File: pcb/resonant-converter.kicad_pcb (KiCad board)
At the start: 2 copper layers, 0 parts

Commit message: PCB: Setup PCB stackup, DRC and pre-defined sizes
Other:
- board outline added: 100 x 100 mm
- copper layers 2 -> 4
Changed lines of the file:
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@@
 	(generator_version "9.0")
 	(general
-		(thickness 1.6)
+		(thickness 1.6062)
 		(legacy_teardrops no)
 	)
@@
 	(layers
 		(0 "F.Cu" signal)
+		(4 "In1.Cu" signal)
+		(6 "In2.Cu" signal)
 		(2 "B.Cu" signal)
 		(9 "F.Adhes" user "F.Adhesive")
@@
 		(43 "User.3" user)
 		(45 "User.4" user)
+		(47 "User.5" user)
+		(49 "User.6" user)
+		(51 "User.7" user)
+		(53 "User.8" user)
+		(55 "User.9" user)
 	)
 	(setup
+		(stackup
+			(layer "F.SilkS"
+				(type "Top Silk Screen")
+				(color "White")
+			)
+			(layer "F.Paste"
+				(type "Top Solder Paste")
+			)
+			(layer "F.Mask"
+				(type "Top Solder Mask")
+				(color "Black")
+				(thickness 0.01)
+			)
+			(layer "F.Cu"
+				(type "copper")
+				(thickness 0.035)
+			)
+			(layer "dielectric 1"
+				(type "prepreg")
+				(color "FR4 natural")
+				(thickness 0.2104)
+				(material "FR4")
+				(epsilon_r 4.4)
+				(loss_tangent 0.02)
+			)
+			(layer "In1.Cu"
+				(type "copper")
+				(thickness 0.0152)
+			)
+			(layer "dielectric 2"
+				(type "core")
+				(color "FR4 natural")
+				(thickness 1.065)
+				(material "FR4")
+				(epsilon_r 4.6)
+				(loss_tangent 0.02)
+			)
+			(layer "In2.Cu"
+				(type "copper")
+				(thickness 0.0152)
+			)
+			(layer "dielectric 3"
+				(type "prepreg")
+				(color "FR4 natural")
+				(thickness 0.2104)
+				(material "FR4")
+				(epsilon_r 4.4)
+				(loss_tangent 0.02)
+			)
+			(layer "B.Cu"
+				(type "copper")
+				(thickness 0.035)
+			)
+			(layer "B.Mask"
+				(type "Bottom Solder Mask")
+				(color "Black")
+				(thickness 0.01)
+			)
+			(layer "B.Paste"
+				(type "Bottom Solder Paste")
+			)
+			(layer "B.SilkS"
+				(type "Bottom Silk Screen")
+				(color "White")
+			)
+			(copper_finish "None")
+			(dielectric_constraints no)
+		)
 		(pad_to_mask_clearance 0)
 		(allow_soldermask_bridges_in_footprints no)
@@
 	)
 	(net 0 "")
+	(gr_rect
+		(start 100 50)
+		(end 200 150)
+		(stroke
+			(width 0.05)
+			(type solid)
+		)
+		(fill no)
+		(layer "Edge.Cuts")
+	)
 	(embedded_fonts no)
 )

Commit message: WIP: Create PCB mockup
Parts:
- added J1: Banana_Jack_Keystone_575-8, DW-footprints:Conn_Banana_Jack_Keystone_575-8, F.Cu at (106.0, 90.0)
- added J2: Banana_Jack_Keystone_575-8, DW-footprints:Conn_Banana_Jack_Keystone_575-8, F.Cu at (106.0, 110.0)
- added J3: Banana_Jack_Keystone_575-8, DW-footprints:Conn_Banana_Jack_Keystone_575-8, F.Cu at (195.0, 90.0)
- added J4: Banana_Jack_Keystone_575-8, DW-footprints:Conn_Banana_Jack_Keystone_575-8, F.Cu at (195.0, 110.0)
- added Q1: SIS472DN-T1-GE3, DW-footprints:PowerPAK-1212-8_Single, F.Cu at (134.4, 100.3)
- added Q2: SIS472DN-T1-GE3, DW-footprints:PowerPAK-1212-8_Single, F.Cu at (134.4, 105.0)
- added Q3: SIS472DN-T1-GE3, DW-footprints:PowerPAK-1212-8_Single, F.Cu at (169.4, 105.0)
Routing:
- added copper zone on In1.Cu, net GND
- added copper zone on In2.Cu, net GND

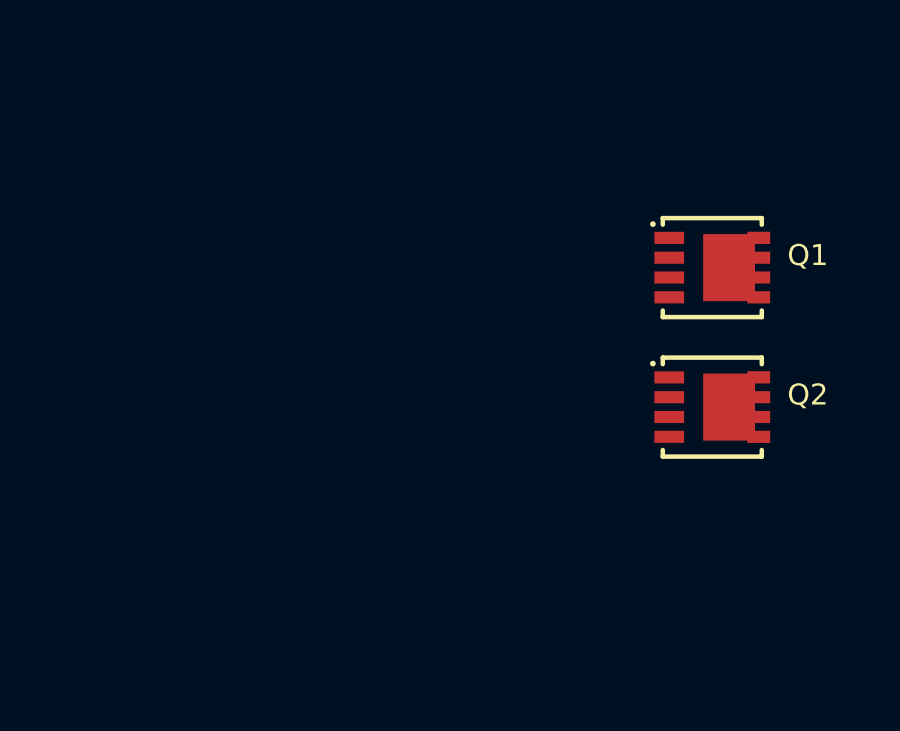
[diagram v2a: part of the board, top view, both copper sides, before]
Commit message: Add LLC controller IC
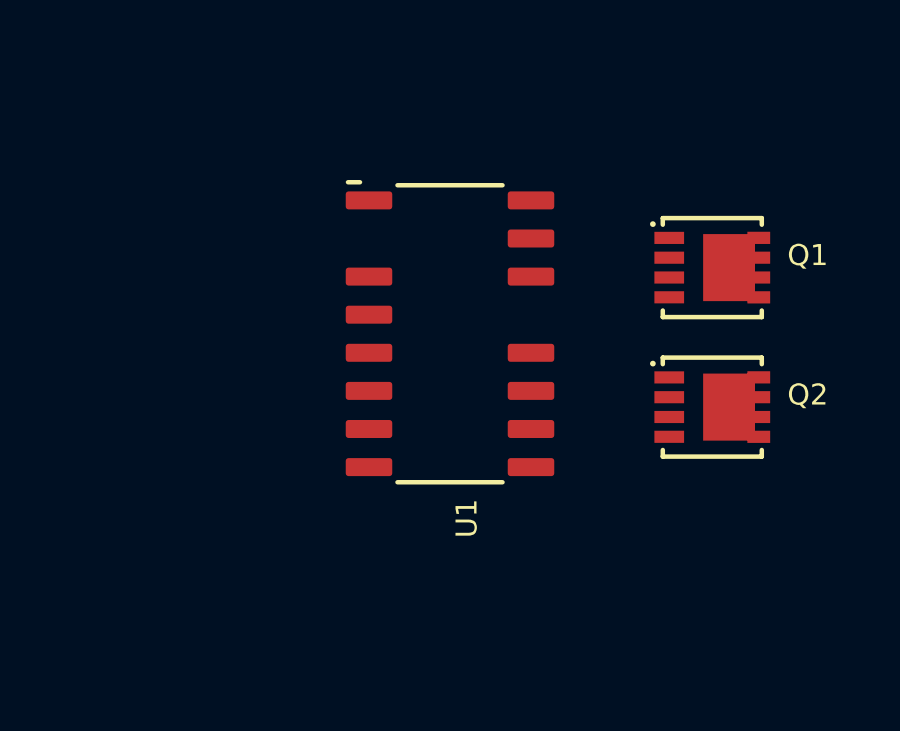
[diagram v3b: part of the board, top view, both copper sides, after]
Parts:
- added U1: UCC256610DDBR, DW-footprints:DDB0014A, F.Cu at (125.7, 102.6)

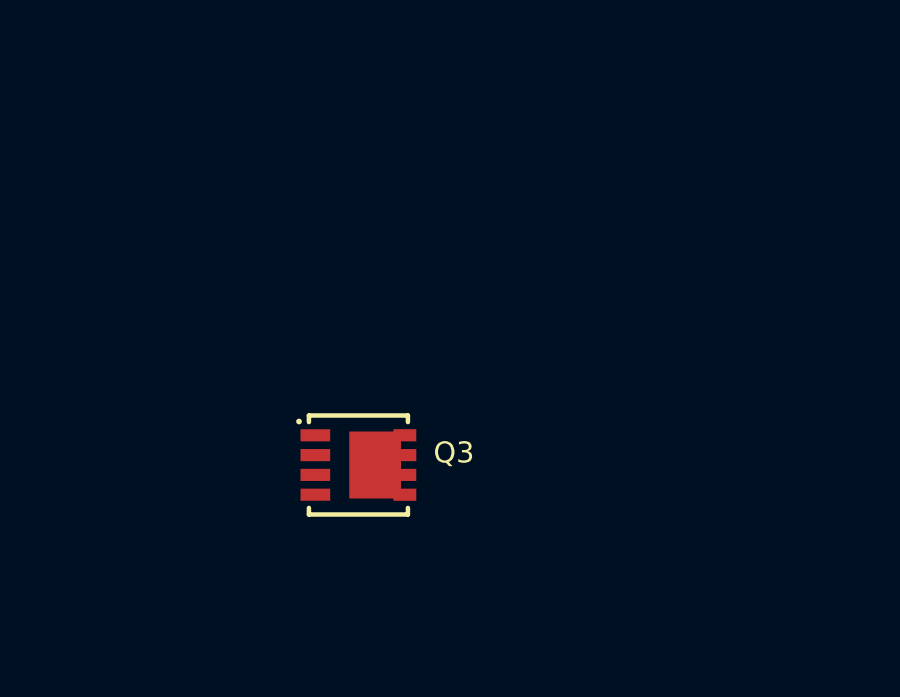
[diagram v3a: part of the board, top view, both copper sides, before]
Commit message: Add output rectifier schottky diodes
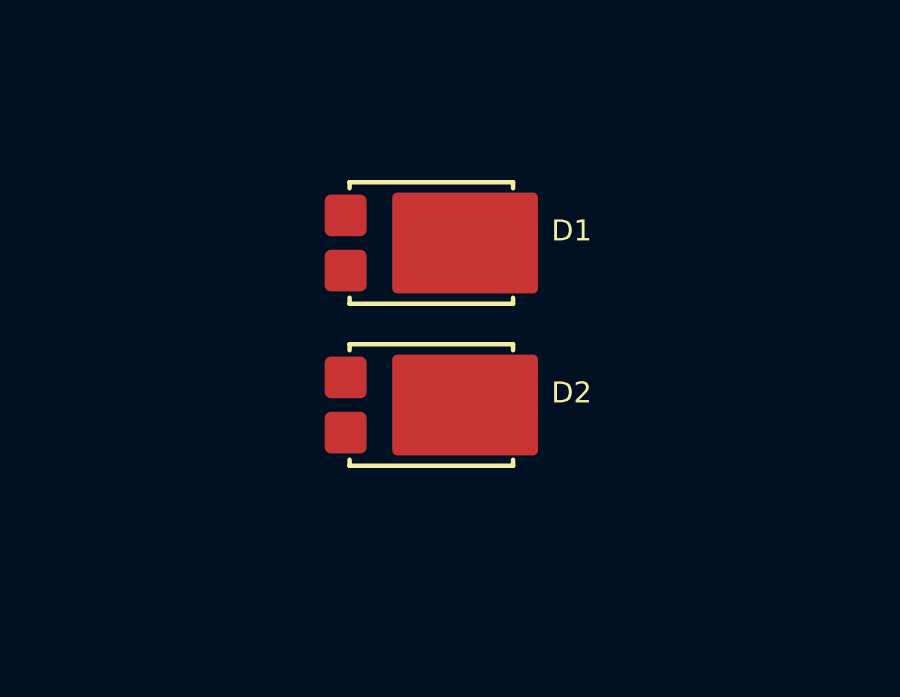
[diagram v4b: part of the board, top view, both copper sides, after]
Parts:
- removed Q3: SIS472DN-T1-GE3, DW-footprints:PowerPAK-1212-8_Single
- added D1: SBRT15U50SP5-13, DW-footprints:PowerDI-5, F.Cu at (171.9, 97.6)
- added D2: SBRT15U50SP5-13, DW-footprints:PowerDI-5, F.Cu at (171.9, 103.0)

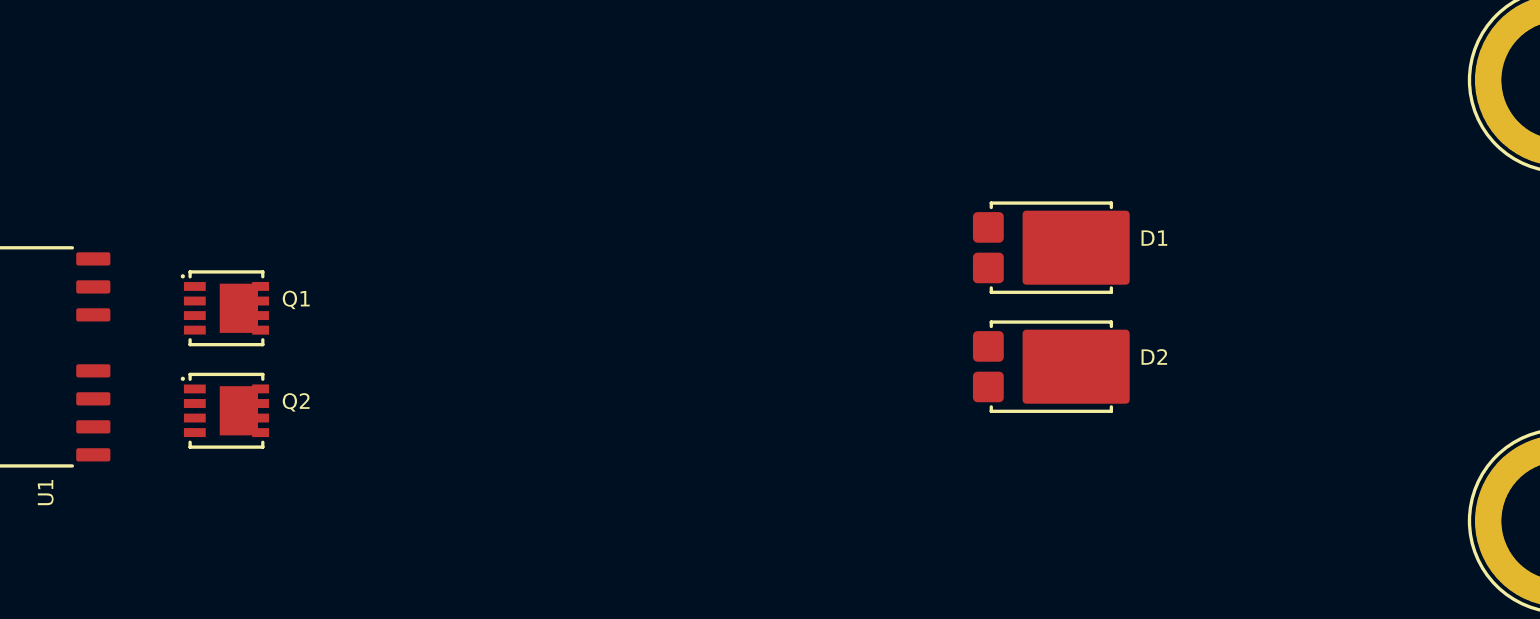
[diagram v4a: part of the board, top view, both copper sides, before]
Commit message: Add synchronous rectifier
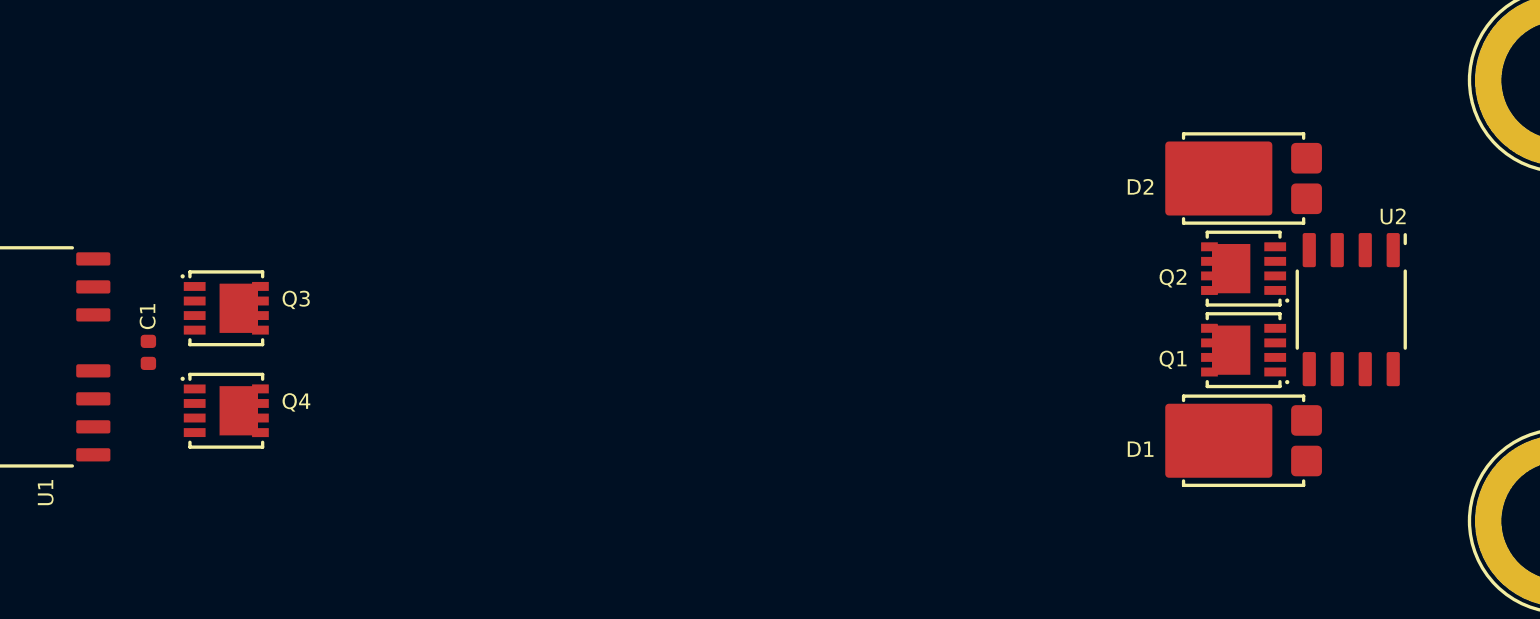
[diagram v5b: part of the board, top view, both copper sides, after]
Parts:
- added C1: C-1u-0402, DW-footprints:C_0402_1005Metric, F.Cu at (130.9, 102.3)
- added Q3: SIS472DN-T1-GE3, DW-footprints:PowerPAK-1212-8_Single, F.Cu at (134.4, 100.3)
- added Q4: SIS472DN-T1-GE3, DW-footprints:PowerPAK-1212-8_Single, F.Cu at (134.4, 105.0)
- added U2: TEA2096T/1J, DW-footprints:SOIC-8_3.9x4.9mm_P1.27mm, F.Cu at (185.5, 100.4)
- moved Q2 46.6 mm to (180.6, 98.5), turned to 180 degrees
- moved Q1 46.2 mm to (180.6, 102.2), turned to 180 degrees
- moved D1 12.4 mm to (180.6, 106.4), turned to 180 degrees
- moved D2 12.2 mm to (180.6, 94.5), turned to 180 degrees
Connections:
- D1 pad 1: unconnected-(D1-C-Pad1) -> Net-(D1-C)
- D1 pad 2: unconnected-(D1-A-Pad2) -> GND
- D2 pad 1: unconnected-(D2-C-Pad1) -> Net-(D2-C)
- D2 pad 2: unconnected-(D2-A-Pad2) -> GND
- J1 pad 1: unconnected-(J1-Pad1) -> VCC
- J2 pad 1: unconnected-(J2-Pad1) -> GNDPWR
- J3 pad 1: unconnected-(J3-Pad1) -> +12V
- Q1 pad 1: Net-(Q1-S-Pad1) -> GND
- Q1 pad 2: Net-(Q1-S-Pad1) -> GND
- Q1 pad 3: Net-(Q1-S-Pad1) -> GND
- Q1 pad 4: unconnected-(Q1-G-Pad4) -> Net-(Q1-G)
- Q1 pad 5: unconnected-(Q1-D-Pad5) -> Net-(D1-C)
- Q2 pad 1: Net-(Q2-S-Pad1) -> GND
- Q2 pad 2: Net-(Q2-S-Pad1) -> GND
- Q2 pad 3: Net-(Q2-S-Pad1) -> GND
- Q2 pad 4: unconnected-(Q2-G-Pad4) -> Net-(Q2-G)
- Q2 pad 5: unconnected-(Q2-D-Pad5) -> Net-(D2-C)
- U1 pad 10: unconnected-(U1-GNDP-Pad10) -> GNDPWR
- U1 pad 11: unconnected-(U1-LO-Pad11) -> Net-(Q4-G)
- U1 pad 14: unconnected-(U1-HB-Pad14) -> Net-(U1-HB)
- U1 pad 15: unconnected-(U1-HO-Pad15) -> Net-(Q3-G)
- U1 pad 16: unconnected-(U1-HS-Pad16) -> Net-(Q4-D)

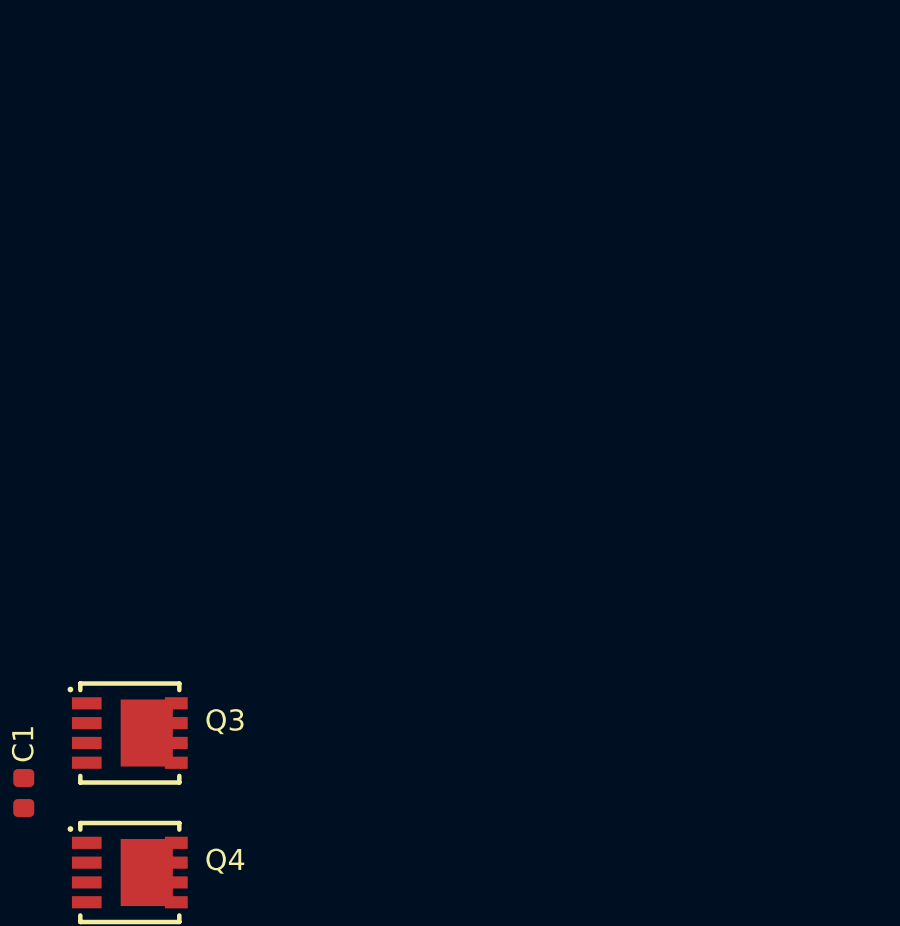
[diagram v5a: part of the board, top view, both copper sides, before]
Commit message: Add resonant inductor and capacitors
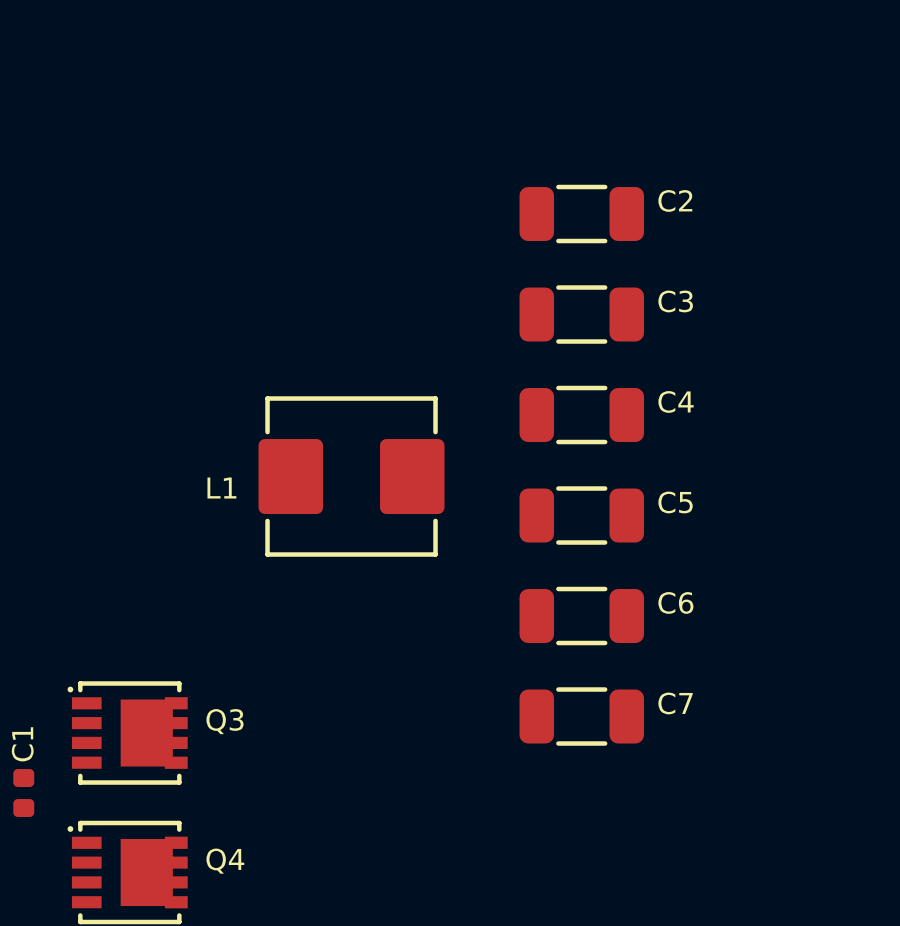
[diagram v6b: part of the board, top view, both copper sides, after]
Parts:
- added C2: C-22n-100V-C0G-1206, DW-footprints:C_1206_3216Metric, F.Cu at (149.5, 83.0)
- added C3: C-22n-100V-C0G-1206, DW-footprints:C_1206_3216Metric, F.Cu at (149.5, 86.4)
- added C4: C-22n-100V-C0G-1206, DW-footprints:C_1206_3216Metric, F.Cu at (149.5, 89.8)
- added C5: C-22n-100V-C0G-1206, DW-footprints:C_1206_3216Metric, F.Cu at (149.5, 93.1)
- added C6: C-22n-100V-C0G-1206, DW-footprints:C_1206_3216Metric, F.Cu at (149.5, 96.5)
- added C7: C-22n-100V-C0G-1206, DW-footprints:C_1206_3216Metric, F.Cu at (149.5, 99.8)
- added L1: L-470n-7A-dehongganying-DH0520H-R47M, DW-footprints:L-dehongganying-DH0520H, F.Cu at (141.8, 91.8)

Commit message: PCB: Update PCB from schematic, add transformer core
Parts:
- added C8: C-1u-0402, DW-footprints:C_0402_1005Metric, F.Cu at (184.0, 115.8)
- added C9: C-22p-0402, DW-footprints:C_0402_1005Metric, F.Cu at (184.0, 117.8)
- added R1: R-1k-0402, DW-footprints:R_0402_1005Metric, F.Cu at (184.0, 119.8)
- added R2: R-1k-0402, DW-footprints:R_0402_1005Metric, F.Cu at (184.0, 121.9)
- added R3: R-1k-0402, DW-footprints:R_0402_1005Metric, F.Cu at (184.0, 124.0)
- added R4: R-1k-0402, DW-footprints:R_0402_1005Metric, F.Cu at (184.0, 126.0)
- added R5: R-1k-0402, DW-footprints:R_0402_1005Metric, F.Cu at (184.0, 128.1)
- added REF**: Core_B66311G0100X187_top, DW-footprints:Core_B66311G0100X187_top, F.Cu at (159.0, 90.0)
- added REF**: Core_B66311G0100X187_bottom, DW-footprints:Core_B66311G0100X187_bottom, F.Cu at (159.0, 90.0)
- added T1: B66206W1110T001, DW-footprints:Bobbin_B66206W1110T001, F.Cu at (159.0, 90.0)
- added U3: INA219BIDCNR, DW-footprints:SOT-23-8, F.Cu at (177.8, 124.7)
- added U4: PC817X2CSP9F, DW-footprints:SMD-4_6.5x4.6mm_P2.54mm, F.Cu at (165.0, 118.0)
- added U5: TL431AIDBVR, DW-footprints:SOT-23-5, F.Cu at (173.2, 124.9)
